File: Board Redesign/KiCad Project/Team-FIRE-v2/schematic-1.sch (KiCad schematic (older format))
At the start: 32 parts, among them J1 SIM_Card, J2 53885-0408, U1 TPS40210DGQR, U2 NCN4555MN, U3 CSD18543Q3A

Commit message: Finished SAMD part selection, fixed alignment on all sheets
- Fixed part selection for all SAMD51 sheet components
- Fixed grid misalignment in SAMD51 components
- Had to remove all SAMD51 additional text for this fix
- Added no connects to unused pins for SAMD51
- Removed component selection comments for all pages
- Add components selected except one or two boost circuit components and the SIM card connector.
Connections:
- wire segments 150 -> 142
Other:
- note removed: "PART SELECTION FINISHED - COLLIN"
- moved on the sheet: C1, C10, C11, C12, C13, C14, C2, C3, C4, C5, C6, C7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

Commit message: Added footprints (& potential one for SIM)
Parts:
- removed D1: D_Schottky, symbol Device:D_Schottky
- removed L1: 24uH, symbol Device:L
- added CR?: B260-13-F, SMB_DIO, symbol sch_diode:B260-13-F
- added L?: IHLP6767GZER220M11, IND_IHLP-6767GZ, symbol Boost_Inductor_24uH:IHLP6767GZER220M11
- added P?: 7111S2015X02LF, FCI_7111S2015X02LF, symbol SIM_Card:7111S2015X02LF
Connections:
- wire segments 142 -> 144
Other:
- note added: "Amphenol part w/ footprint for SIM holder...\n but haven't found a datasheet yet and the pins aren't labelled. \nWe could probably figure it out from the general \nSIM specifications though"
- note removed: "FIND COMPONENT"
- note removed: "FIND COMPONENTS"
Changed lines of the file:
@@
 EESchema Schematic File Version 4
-LIBS:Team-FIRE-v2-cache
 EELAYER 30 0
 EELAYER END
@@
 Wire Wire Line
 	4050 2500 4600 2500
-$Comp
-L Device:L L1
-U 1 1 5ECDA0A4
-P 5450 1450
-F 0 "L1" H 5503 1496 50  0000 L CNN
-F 1 "24uH" H 5503 1405 50  0000 L CNN
-F 2 "" H 5450 1450 50  0001 C CNN
-F 3 "~" H 5450 1450 50  0001 C CNN
-	1    5450 1450
-	1    0    0    -1
-$EndComp
 Wire Wire Line
 	1200 2100 1200 2450
@@
 	1    0    0    -1
 $EndComp
-$Comp
-L Device:D_Schottky D1
-U 1 1 5EDFAAE4
-P 6000 1750
-F 0 "D1" H 6000 1534 50  0000 C CNN
-F 1 "D_Schottky" H 6000 1625 50  0000 C CNN
-F 2 "" H 6000 1750 50  0001 C CNN
-F 3 "~" H 6000 1750 50  0001 C CNN
-	1    6000 1750
-	-1   0    0    1
-$EndComp
-Wire Wire Line
-	5850 1750 5450 1750
-Connection ~ 5450 1750
 Wire Wire Line
 	5450 1750 5450 1900
@@
 Wire Wire Line
 	6050 2850 6150 2850
-Wire Wire Line
-	6150 1750 6400 1750
 Wire Wire Line
 	6400 1750 6400 2850
@@
 	4700 1100 4700 1200
 Wire Wire Line
-	5450 1600 5450 1750
-Wire Wire Line
-	5450 1300 5450 1200
-Wire Wire Line
-	5450 1200 5000 1200
-Connection ~ 5000 1200
+	5550 1000 5550 900
 Wire Wire Line
 	4700 1200 5000 1200
@@
 	1    0    0    -1
 $EndComp
-Text Notes 6600 1300 2    79   ~ 16
-FIND COMPONENTS
-Text Notes 5200 4750 2    79   ~ 16
-FIND COMPONENT
 $Comp
 L Team-FIRE:EEE-FK1H390SV C11
@@
 Wire Wire Line
 	6500 1750 6400 1750
+Wire Wire Line
+	2900 5050 2900 4650
+Wire Notes Line
+	6850 800  6850 4150
+Wire Notes Line
+	750  4150 750  800
+$Comp
+L Boost_Inductor_24uH:IHLP6767GZER220M11 L?
+U 1 1 5EB30B50
+P 5550 1000
+F 0 "L?" V 5800 1150 60  0000 L CNN
+F 1 "IHLP6767GZER220M11" V 5900 1150 60  0000 L CNN
+F 2 "IND_IHLP-6767GZ" H 5825 715 60  0001 C CNN
+F 3 "" H 5550 1000 60  0000 C CNN
+	1    5550 1000
+	0    1    1    0
+$EndComp
+Wire Wire Line
+	5000 900  5000 1200
+Wire Wire Line
+	5000 900  5550 900
+Connection ~ 5000 1200
+Wire Wire Line
+	5550 1600 5550 1750
+Wire Wire Line
+	5550 1750 5450 1750
+$Comp
+L sch_diode:B260-13-F CR?
+U 1 1 5EB57D9C
+P 5800 1750
+F 0 "CR?" H 6000 2013 60  0000 C CNN
+F 1 "B260-13-F" H 6000 1907 60  0000 C CNN
+F 2 "SMB_DIO" H 6000 1390 60  0001 C CNN
+F 3 "" H 5800 1750 60  0000 C CNN
+	1    5800 1750
+	1    0    0    -1
+$EndComp
+Wire Notes Line
+	6850 4150 750  4150
+Wire Wire Line
+	5800 1750 5550 1750
+Connection ~ 5550 1750
+Wire Wire Line
+	6200 1750 6400 1750
 Connection ~ 6400 1750
-Wire Wire Line
-	2900 5050 2900 4650
-Wire Notes Line
-	6850 800  6850 4150
-Wire Notes Line
-	6850 4150 750  4150
-Wire Notes Line
-	750  4150 750  800
+$Comp
+L SIM_Card:7111S2015X02LF P?
+U 1 1 5EB9D6BE
+P 4350 6700
+F 0 "P?" H 4630 6746 50  0000 L CNN
+F 1 "7111S2015X02LF" H 4630 6655 50  0000 L CNN
+F 2 "FCI_7111S2015X02LF" H 4350 6700 50  0001 L BNN
+F 3 "Framatome/Amphenol" H 4350 6700 50  0001 L BNN
+	1    4350 6700
+	1    0    0    -1
+$EndComp
+Text Notes 3550 7450 0    50   ~ 0
+Amphenol part w/ footprint for SIM holder...\n but haven't found a datasheet yet and the pins aren't labelled. \nWe could probably figure it out from the general \nSIM specifications though
 $EndSCHEMATC

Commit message: Fixed some library problems
- Deleted uselss import files
- Fixed B26013F library files
- Fixed IHLP6767GZER220M11 library files
- Fixed weird library reference for inductor, transistor, and diode
- Imported shelby's files to the Team-FIRE library
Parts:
- removed CR?: B260-13-F, SMB_DIO, symbol sch_diode:B260-13-F
- removed L?: IHLP6767GZER220M11, IND_IHLP-6767GZ, symbol Boost_Inductor_24uH:IHLP6767GZER220M11
- added CR?: B260-13-F, SMB_DIO, symbol Team-FIRE:B260-13-F
- added L?: 24uH, Team-FIRE:IHLP6767GZER220M11, symbol Team-FIRE:IHLP6767GZER220M11
- U3: symbol Boost_switch:CSD18543Q3A -> Team-FIRE:CSD18543Q3A
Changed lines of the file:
@@
 EESchema Schematic File Version 4
+LIBS:Team-FIRE-v2-cache
 EELAYER 30 0
 EELAYER END
@@
 	4150 2000 4150 2200
 $Comp
-L Boost_switch:CSD18543Q3A U3
+L Team-FIRE:CSD18543Q3A U3
 U 1 1 5EC35A93
 P 5350 2200
+AR Path="/5EC35A93" Ref="U3"  Part="1"
+AR Path="/5E4D0D8F/5EC35A93" Ref="U3"  Part="1"
 F 0 "U3" H 5630 2231 60  0000 L CNN
 F 1 "CSD18543Q3A" H 5630 2125 60  0000 L CNN
@@
 Wire Wire Line
 	4700 1100 4700 1200
-Wire Wire Line
-	5550 1000 5550 900
 Wire Wire Line
 	4700 1200 5000 1200
@@
 Wire Notes Line
 	750  4150 750  800
-$Comp
-L Boost_Inductor_24uH:IHLP6767GZER220M11 L?
-U 1 1 5EB30B50
-P 5550 1000
-F 0 "L?" V 5800 1150 60  0000 L CNN
-F 1 "IHLP6767GZER220M11" V 5900 1150 60  0000 L CNN
-F 2 "IND_IHLP-6767GZ" H 5825 715 60  0001 C CNN
-F 3 "" H 5550 1000 60  0000 C CNN
-	1    5550 1000
-	0    1    1    0
-$EndComp
-Wire Wire Line
-	5000 900  5000 1200
-Wire Wire Line
-	5000 900  5550 900
 Connection ~ 5000 1200
 Wire Wire Line
-	5550 1600 5550 1750
-Wire Wire Line
 	5550 1750 5450 1750
-$Comp
-L sch_diode:B260-13-F CR?
-U 1 1 5EB57D9C
-P 5800 1750
-F 0 "CR?" H 6000 2013 60  0000 C CNN
-F 1 "B260-13-F" H 6000 1907 60  0000 C CNN
-F 2 "SMB_DIO" H 6000 1390 60  0001 C CNN
-F 3 "" H 5800 1750 60  0000 C CNN
-	1    5800 1750
-	1    0    0    -1
-$EndComp
 Wire Notes Line
 	6850 4150 750  4150
@@
 Text Notes 3550 7450 0    50   ~ 0
 Amphenol part w/ footprint for SIM holder...\n but haven't found a datasheet yet and the pins aren't labelled. \nWe could probably figure it out from the general \nSIM specifications though
+$Comp
+L Team-FIRE:B260-13-F CR?
+U 1 1 5EB38CCA
+P 5800 1750
+F 0 "CR?" H 6000 2013 60  0000 C CNN
+F 1 "B260-13-F" H 6000 1907 60  0000 C CNN
+F 2 "SMB_DIO" H 6000 1390 60  0001 C CNN
+F 3 "https://www.diodes.com/assets/Datasheets/ds13004.pdf" H 5800 1750 60  0001 C CNN
+F 4 "B260-13-F" H 6050 1500 50  0001 C CNN "MPN"
+F 5 "Diodes Incorporated" H 6200 1300 50  0001 C CNN "Manufacturer"
+F 6 "Digikey" H 5950 1100 50  0001 C CNN "Supplier"
+F 7 "B260-FDICT-ND" H 6150 1200 50  0001 C CNN "Supplier PN"
+F 8 "https://www.digikey.ca/product-detail/en/diodes-incorporated/B260-13-F/B260-FDICT-ND/815329" H 7800 1000 50  0001 C CNN "Link"
+F 9 "Schottky Diode" H 6100 700 50  0001 C CNN "Type"
+F 10 "60 V" H 5900 900 50  0001 C CNN "Voltage Rating"
+F 11 "2 A" H 5900 800 50  0001 C CNN "Current Rating"
+	1    5800 1750
+	1    0    0    -1
+$EndComp
+$Comp
+L Team-FIRE:IHLP6767GZER220M11 L?
+U 1 1 5EB4A6BF
+P 5550 1050
+F 0 "L?" V 5800 1200 60  0000 L CNN
+F 1 "24uH" V 5900 1200 60  0000 L CNN
+F 2 "Team-FIRE:IHLP6767GZER220M11" H 6350 950 60  0001 C CNN
+F 3 "http://www.vishay.com/docs/34282/ihlp-6767gz-11.pdf" H 5550 1050 60  0001 C CNN
+F 4 "IHLP6767GZER220M11" H 6000 750 50  0001 C CNN "MPN"
+F 5 "Vishay Dale" H 5800 850 50  0001 C CNN "Manufacturer"
+F 6 "Digikey" H 5700 650 50  0001 C CNN "Supplier"
+F 7 "541-1288-1-ND" H 5900 550 50  0001 C CNN "Supplier PN"
+F 8 "https://www.digikey.com/product-detail/en/vishay-dale/IHLP6767GZER220M11/541-1288-1-ND/2139414" H 7650 450 50  0001 C CNN "Link"
+F 9 "Fixed shielded inductor" H 6000 350 50  0001 C CNN "Type"
+F 10 "20%" H 5650 250 50  0001 C CNN "Tolerance"
+F 11 "12 A" H 5650 150 50  0001 C CNN "Current Rating"
+	1    5550 1050
+	0    1    1    0
+$EndComp
+Wire Wire Line
+	5550 1650 5550 1750
+Wire Wire Line
+	5550 1050 5550 950
+Wire Wire Line
+	5550 950  5000 950
+Wire Wire Line
+	5000 950  5000 1200
 $EndSCHEMATC

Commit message: Finished schematic
- Added 47338-2001 symbol, footprint, and model to schematic
- Added 47338-2001 to Team-FIRE library
- Created custom SIM card holder symbol
- Added all component description values for SIM card holder
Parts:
- removed J1: SIM_Card, Package_DFN_QFN:QFN-16-1EP_3x3mm_P0.5mm_EP1.75x1.75mm, symbol Connector:SIM_Card
- removed P?: 7111S2015X02LF, FCI_7111S2015X02LF, symbol SIM_Card:7111S2015X02LF
- added J?: 47388-2001, Team-FIRE:473882001, symbol Team-FIRE:47388-2001
- gave numbers to parts that had none: 2
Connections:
- net GND: now also J?.6 (GND), J?.7 (CASE), J?.8 (CASE)
- net SIM_CLOCK: now also J?.1 (CLK)
- net SIM_IO: now also J?.4 (I/O)
- net SIM_RESET: now also J?.2 (RST)
- net SIM_VCC: now also J?.3 (VCC)
- no-connect marks 13 -> 12
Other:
- note removed: "Amphenol part w/ footprint for SIM holder...\n but haven't found a datasheet yet and the pins aren't labelled. \nWe could probably figure it out from the general \nSIM specifications though"
- moved on the sheet: C12, C14, C6

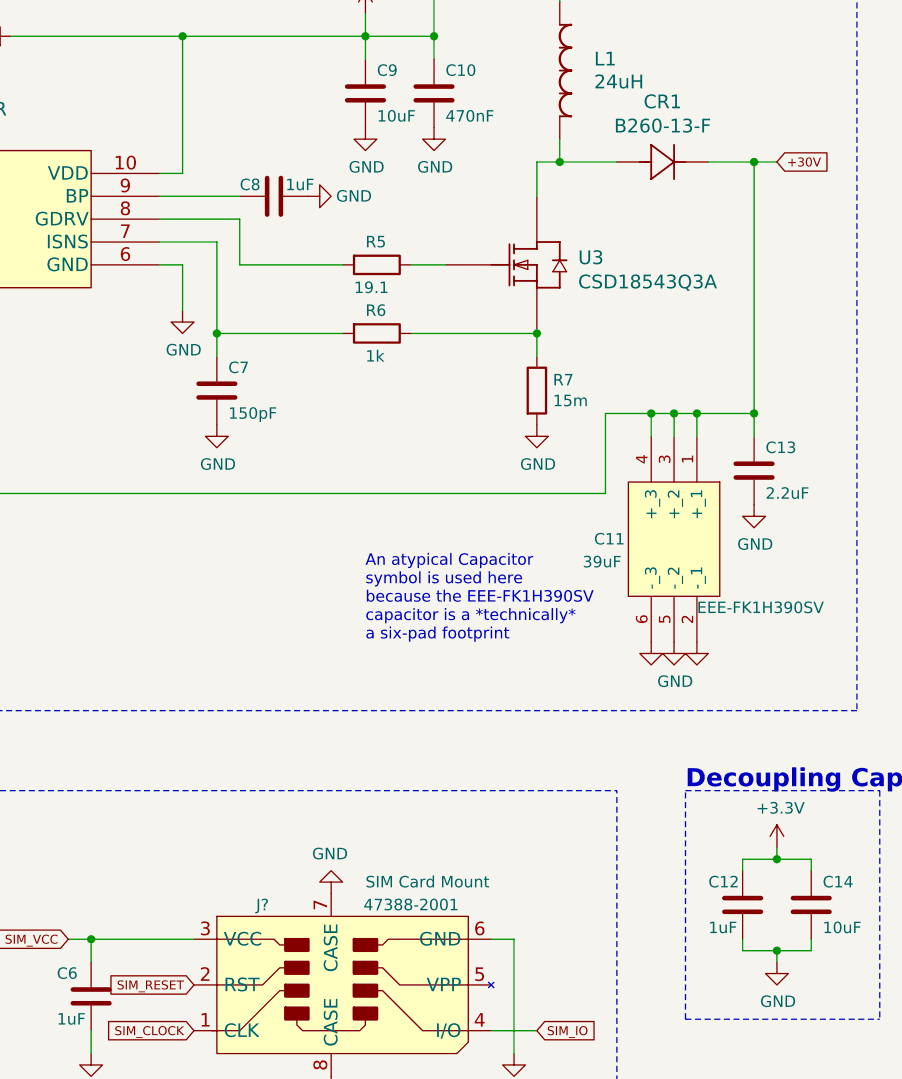
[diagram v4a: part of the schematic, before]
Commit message: Replaced transistor symbol, and footprint
- Had to replace the CSD18543Q3AT transistor with a custom symbol, footprint and 3D model to account for the 9-pin package it resides in (not a 3 pin as the symbol depicts)
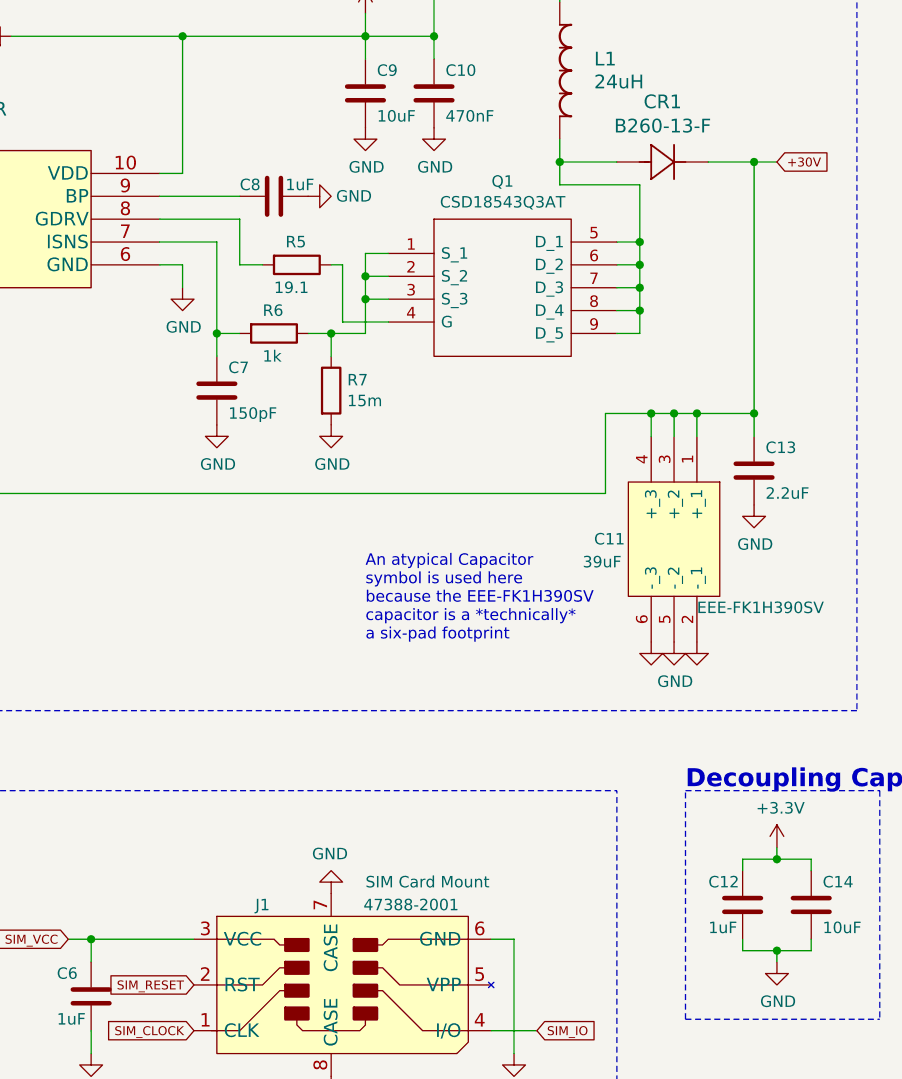
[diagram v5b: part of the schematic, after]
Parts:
- removed U3: CSD18543Q3A, Package_SON:VSON-8_3.3x3.3mm_P0.65mm_NexFET, symbol Team-FIRE:CSD18543Q3A
- added Q1: CSD18543Q3AT, Team-FIRE:CSD18543Q3AT, symbol Team-FIRE:CSD18543Q3AT
- CR1: footprint SMB_DIO -> Team-FIRE:DIOM5336X250N
- gave numbers to parts that had none: 1
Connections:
- net at CR1.2, L1.1: now also Q1.5 (D_1), Q1.6 (D_2), Q1.7 (D_3), Q1.8 (D_4), Q1.9 (D_5)
- net at R5.1: now also Q1.4 (G)
- net at R6.1, R7.1: now also Q1.1 (S_1), Q1.2 (S_2), Q1.3 (S_3)
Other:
- moved on the sheet: R5, R6, R7

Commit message: Finished PCB
- Added various 3D models for a complete 3D visualization of the PCB
- Generated a finalized netlist
- Fixed misnamed net from IR_SIM_RST to IR_SIM_RESET
- Finished all component placement for the PCB; the only work remaining are the mounting holes, and the grounding vias for the IRIDIUM
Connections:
- net IR_SIM_RST is gone; now on net IR_SIM_RESET: J2.26 (SIM_RESET)
- net IR_SIM_CLK renamed IR_SIM_CLOCK
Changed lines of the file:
@@
 RF_EN
 Text GLabel 7750 2500 0    39   Input ~ 0
-IR_SIM_RST
+IR_SIM_RESET
 Text GLabel 7750 2400 0    39   Input ~ 0
-IR_SIM_CLK
+IR_SIM_CLOCK
 Text GLabel 7750 2300 0    39   Input ~ 0
 DTR
@@
 IR_SIM_RESET
 Text GLabel 1400 5450 0    39   Input ~ 0
-IR_SIM_CLK
+IR_SIM_CLOCK
 Text GLabel 1400 5550 0    39   Input ~ 0
 IR_SIM_IO

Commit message: Minor changes
- Made some little changes; not really important.
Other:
- moved on the sheet: CR1, L1, R3
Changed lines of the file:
@@
 L Device:R R3
 U 1 1 5EB0327A
-P 3000 1200
+P 2800 1200
 AR Path="/5E4D0D8F/5EB0327A" Ref="R3"  Part="1"
 AR Path="/5E759307/5EB0327A" Ref="R?"  Part="1"
-F 0 "R3" V 3100 1150 50  0000 L CNN
-F 1 "301k" V 2900 1100 50  0000 L CNN
-F 2 "Resistor_SMD:R_0603_1608Metric" V 2930 1200 50  0001 C CNN
-F 3 "https://www.mouser.com/datasheet/2/427/crcwhpe3-1713858.pdf" H 3000 1200 50  0001 C CNN
-F 4 "CRCW0603301KFKEAHP" V 3000 1200 50  0001 C CNN "MPN"
-F 5 "Thick Film Resistors" V 3000 1200 50  0001 C CNN "Type"
-F 6 "75 V" V 3000 1200 50  0001 C CNN "Voltage Rating"
-F 7 "Vishay" V 3000 1200 50  0001 C CNN "Manufacturer"
-F 8 "Mouser" V 3000 1200 50  0001 C CNN "Supplier"
-F 9 "https://www.mouser.com/ProductDetail/Vishay-Dale/CRCW0603301KFKEAHP?qs=sGAEpiMZZMtlubZbdhIBILDMOtf4qnQoMDmfFrlZC70%3D" V 3000 1200 50  0001 C CNN "Link"
-F 10 "1%" V 3000 1200 50  0001 C CNN "Tolerance"
-F 11 "AEC-Q200" V 3000 1200 50  0001 C CNN "Qualification"
-	1    3000 1200
+F 0 "R3" V 2900 1150 50  0000 L CNN
+F 1 "301k" V 2700 1100 50  0000 L CNN
+F 2 "Resistor_SMD:R_0603_1608Metric" V 2730 1200 50  0001 C CNN
+F 3 "https://www.mouser.com/datasheet/2/427/crcwhpe3-1713858.pdf" H 2800 1200 50  0001 C CNN
+F 4 "CRCW0603301KFKEAHP" V 2800 1200 50  0001 C CNN "MPN"
+F 5 "Thick Film Resistors" V 2800 1200 50  0001 C CNN "Type"
+F 6 "75 V" V 2800 1200 50  0001 C CNN "Voltage Rating"
+F 7 "Vishay" V 2800 1200 50  0001 C CNN "Manufacturer"
+F 8 "Mouser" V 2800 1200 50  0001 C CNN "Supplier"
+F 9 "https://www.mouser.com/ProductDetail/Vishay-Dale/CRCW0603301KFKEAHP?qs=sGAEpiMZZMtlubZbdhIBILDMOtf4qnQoMDmfFrlZC70%3D" V 2800 1200 50  0001 C CNN "Link"
+F 10 "1%" V 2800 1200 50  0001 C CNN "Tolerance"
+F 11 "AEC-Q200" V 2800 1200 50  0001 C CNN "Qualification"
+	1    2800 1200
 	0    -1   -1   0
 $EndComp
@@
 U 1 1 5EAFAF05
 P 1800 1800
-F 0 "U1" H 2800 2187 60  0000 C CNN
-F 1 "TPS40210DGQR" H 2800 2081 60  0000 C CNN
+F 0 "U1" H 2200 1950 60  0000 C CNN
+F 1 "TPS40210DGQR" H 3150 1950 60  0000 C CNN
 F 2 "Team-FIRE:TPS40210DGQR" H 2900 2000 60  0001 C CNN
 F 3 "http://www.ti.com/general/docs/suppproductinfo.tsp?distId=26&gotoUrl=http%3A%2F%2Fwww.ti.com%2Flit%2Fgpn%2Ftps40210" H 2800 2081 60  0001 C CNN
@@
 	1800 1800 1700 1800
 Wire Wire Line
-	1700 1200 2850 1200
+	1700 1200 2650 1200
 Wire Wire Line
 	3800 1800 3900 1800
 Wire Wire Line
 	3900 1800 3900 1200
-Wire Wire Line
-	3900 1200 3150 1200
 Wire Wire Line
 	3800 1900 4150 1900
@@
 Wire Notes Line
 	750  4150 750  800
-Connection ~ 5000 1200
 Wire Notes Line
 	6850 4150 750  4150
-Wire Wire Line
-	5800 1750 5550 1750
-Wire Wire Line
-	6200 1750 6400 1750
-Connection ~ 6400 1750
 $Comp
 L Team-FIRE:B260-13-F CR1
 U 1 1 5EB38CCA
-P 5800 1750
-F 0 "CR1" H 6000 2013 60  0000 C CNN
-F 1 "B260-13-F" H 6000 1907 60  0000 C CNN
-F 2 "Team-FIRE:DIOM5336X250N" H 6000 1390 60  0001 C CNN
-F 3 "https://www.diodes.com/assets/Datasheets/ds13004.pdf" H 5800 1750 60  0001 C CNN
-F 4 "B260-13-F" H 6050 1500 50  0001 C CNN "MPN"
-F 5 "Diodes Incorporated" H 6200 1300 50  0001 C CNN "Manufacturer"
-F 6 "Digikey" H 5950 1100 50  0001 C CNN "Supplier"
-F 7 "B260-FDICT-ND" H 6150 1200 50  0001 C CNN "Supplier PN"
-F 8 "https://www.digikey.ca/product-detail/en/diodes-incorporated/B260-13-F/B260-FDICT-ND/815329" H 7800 1000 50  0001 C CNN "Link"
-F 9 "Schottky Diode" H 6100 700 50  0001 C CNN "Type"
-F 10 "60 V" H 5900 900 50  0001 C CNN "Voltage Rating"
-F 11 "2 A" H 5900 800 50  0001 C CNN "Current Rating"
-	1    5800 1750
+P 5950 1750
+F 0 "CR1" H 6050 2000 60  0000 C CNN
+F 1 "B260-13-F" H 6250 1900 60  0000 C CNN
+F 2 "Team-FIRE:DIOM5336X250N" H 6150 1390 60  0001 C CNN
+F 3 "https://www.diodes.com/assets/Datasheets/ds13004.pdf" H 5950 1750 60  0001 C CNN
+F 4 "B260-13-F" H 6200 1500 50  0001 C CNN "MPN"
+F 5 "Diodes Incorporated" H 6350 1300 50  0001 C CNN "Manufacturer"
+F 6 "Digikey" H 6100 1100 50  0001 C CNN "Supplier"
+F 7 "B260-FDICT-ND" H 6300 1200 50  0001 C CNN "Supplier PN"
+F 8 "https://www.digikey.ca/product-detail/en/diodes-incorporated/B260-13-F/B260-FDICT-ND/815329" H 7950 1000 50  0001 C CNN "Link"
+F 9 "Schottky Diode" H 6250 700 50  0001 C CNN "Type"
+F 10 "60 V" H 6050 900 50  0001 C CNN "Voltage Rating"
+F 11 "2 A" H 6050 800 50  0001 C CNN "Current Rating"
+	1    5950 1750
 	1    0    0    -1
 $EndComp
@@
 L Team-FIRE:IHLP6767GZER220M11 L1
 U 1 1 5EB4A6BF
-P 5550 1050
-F 0 "L1" V 5800 1200 60  0000 L CNN
-F 1 "24uH" V 5900 1200 60  0000 L CNN
-F 2 "Team-FIRE:IHLP6767GZER220M11" H 6350 950 60  0001 C CNN
-F 3 "http://www.vishay.com/docs/34282/ihlp-6767gz-11.pdf" H 5550 1050 60  0001 C CNN
-F 4 "IHLP6767GZER220M11" H 6000 750 50  0001 C CNN "MPN"
-F 5 "Vishay Dale" H 5800 850 50  0001 C CNN "Manufacturer"
-F 6 "Digikey" H 5700 650 50  0001 C CNN "Supplier"
-F 7 "541-1288-1-ND" H 5900 550 50  0001 C CNN "Supplier PN"
-F 8 "https://www.digikey.com/product-detail/en/vishay-dale/IHLP6767GZER220M11/541-1288-1-ND/2139414" H 7650 450 50  0001 C CNN "Link"
-F 9 "Fixed shielded inductor" H 6000 350 50  0001 C CNN "Type"
-F 10 "20%" H 5650 250 50  0001 C CNN "Tolerance"
-F 11 "12 A" H 5650 150 50  0001 C CNN "Current Rating"
-	1    5550 1050
-	0    1    1    0
-$EndComp
-Wire Wire Line
-	5550 1650 5550 1750
-Wire Wire Line
-	5550 1050 5550 950
-Wire Wire Line
-	5550 950  5000 950
-Wire Wire Line
-	5000 950  5000 1200
-Wire Wire Line
-	2100 2550 1700 2550
-Wire Wire Line
-	1700 2550 1700 2450
-Wire Wire Line
-	2100 2550 2100 3000
+P 5100 1200
+F 0 "L1" V 5350 1350 60  0000 L CNN
+F 1 "24uH" V 5450 1350 60  0000 L CNN
+F 2 "Team-FIRE:IHLP6767GZER220M11" H 5900 1100 60  0001 C CNN
+F 3 "http://www.vishay.com/docs/34282/ihlp-6767gz-11.pdf" H 5100 1200 60  0001 C CNN
+F 4 "IHLP6767GZER220M11" H 5550 900 50  0001 C CNN "MPN"
+F 5 "Vishay Dale" H 5350 1000 50  0001 C CNN "Manufacturer"
+F 6 "Digikey" H 5250 800 50  0001 C CNN "Supplier"
+F 7 "541-1288-1-ND" H 5450 700 50  0001 C CNN "Supplier PN"
+F 8 "https://www.digikey.com/product-detail/en/vishay-dale/IHLP6767GZER220M11/541-1288-1-ND/2139414" H 7200 600 50  0001 C CNN "Link"
+F 9 "Fixed shielded inductor" H 5550 500 50  0001 C CNN "Type"
+F 10 "20%" H 5200 400 50  0001 C CNN "Tolerance"
+F 11 "12 A" H 5200 300 50  0001 C CNN "Current Rating"
+	1    5100 1200
+	1    0    0    -1
+$EndComp
+Wire Wire Line
+	2100 2700 1700 2700
 Connection ~ 1700 2450
 Wire Wire Line
@@
 U 1 1 5EBA2567
 P 4800 2100
-F 0 "Q1" H 5300 2365 50  0000 C CNN
-F 1 "CSD18543Q3AT" H 5300 2274 50  0000 C CNN
+F 0 "Q1" H 5300 2250 50  0000 C CNN
+F 1 "CSD18543Q3AT" H 5300 1550 50  0000 C CNN
 F 2 "Team-FIRE:CSD18543Q3AT" H 5650 2200 50  0001 L CNN
 F 3 "http://www.ti.com/lit/gpn/csd18543q3a" H 5650 2100 50  0001 L CNN
@@
 	5900 2100 5900 2200
 Connection ~ 5900 2200
-Wire Wire Line
-	5550 1750 5550 1850
-Wire Wire Line
-	5550 1850 5900 1850
-Wire Wire Line
-	5900 1850 5900 2100
-Connection ~ 5550 1750
 Connection ~ 5900 2100
 Wire Wire Line
@@
 Wire Wire Line
 	4600 2200 4550 2200
+Wire Wire Line
+	2100 2700 2100 3000
+Wire Wire Line
+	1700 2450 1700 2700
+Wire Wire Line
+	5100 1200 5000 1200
+Connection ~ 5000 1200
+Wire Wire Line
+	2950 1200 3900 1200
+Wire Wire Line
+	6350 1750 6400 1750
+Connection ~ 6400 1750
+Wire Wire Line
+	5950 1750 5900 1750
+Wire Wire Line
+	5900 1750 5900 1200
+Connection ~ 5900 1750
+Wire Wire Line
+	5700 1200 5900 1200
+Wire Wire Line
+	5900 1750 5900 2100
 $EndSCHEMATC
